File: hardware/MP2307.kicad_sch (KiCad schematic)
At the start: 13 parts, among them U5 MP2307DN-LF-Z

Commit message: ldo
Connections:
- net +12V_UPS renamed IN
- net +3.3V_UPS renamed OUT
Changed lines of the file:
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@@
+	)
+	(junction
+		(at 83.82 67.31)
+		(diameter 0)
+		(color 0 0 0 0)
 	)
 	(junction
@@
 	)
 	(junction
-		(at 128.27 67.31)
-		(diameter 0)
-		(color 0 0 0 0)
-	)
-	(junction
 		(at 152.4 83.82)
 		(diameter 0)
@@
 	(wire
 		(pts
-			(xy 128.27 63.5) (xy 128.27 67.31)
+			(xy 74.93 67.31) (xy 83.82 67.31)
 		)
 		(stroke
@@
 			(width 0)
 			(type default)
+		)
+	)
+	(hierarchical_label "OUT"
+		(shape output)
+		(at 194.31 80.01 0)
+		(effects
+			(font
+				(size 1.27 1.27)
+			)
+			(justify left)
+		)
+	)
+	(hierarchical_label "IN"
+		(shape input)
+		(at 74.93 67.31 180)
+		(effects
+			(font
+				(size 1.27 1.27)
+			)
+			(justify right)
 		)
 	)
@@
 	)
 	(symbol
-		(lib_id "power:+12V")
-		(at 128.27 63.5 0)
-		(unit 1)
-		(exclude_from_sim no)
-		(in_bom yes)
-		(on_board yes)
-		(dnp no)
-		(property "Reference" "#PWR018"
-			(at 128.27 67.31 0)
-			(effects
-				(font
-					(size 1.27 1.27)
-				)
-				(hide yes)
-			)
-		)
-		(property "Value" "+12V_UPS"
-			(at 117.094 61.976 0)
-			(effects
-				(font
-					(size 1.27 1.27)
-				)
-				(justify left)
-			)
-		)
-		(property "Footprint" ""
-			(at 128.27 63.5 0)
-			(effects
-				(font
-					(size 1.27 1.27)
-				)
-				(hide yes)
-			)
-		)
-		(property "Datasheet" ""
-			(at 128.27 63.5 0)
-			(effects
-				(font
-					(size 1.27 1.27)
-				)
-				(hide yes)
-			)
-		)
-		(property "Description" "Power symbol creates a global label with name \"+12V\""
-			(at 128.27 63.5 0)
-			(effects
-				(font
-					(size 1.27 1.27)
-				)
-				(hide yes)
-			)
-		)
-		(pin "1"
-		)
-		(instances
-			(project "NosVolt"
-				(path "/2a3ef4c2-927a-45cd-a4f2-5ee83a7e9444/32fe5c1b-d6e5-49ce-a57a-909ff60d86f6"
-					(reference "#PWR018")
-					(unit 1)
-				)
-			)
-		)
-	)
-	(symbol
 		(lib_id "Device:R")
 		(at 152.4 92.71 180)
@@
 	)
 	(symbol
-		(lib_id "power:+3.3V")
-		(at 194.31 80.01 270)
-		(unit 1)
-		(exclude_from_sim no)
-		(in_bom yes)
-		(on_board yes)
-		(dnp no)
-		(property "Reference" "#PWR022"
-			(at 190.5 80.01 0)
-			(effects
-				(font
-					(size 1.27 1.27)
-				)
-				(hide yes)
-			)
-		)
-		(property "Value" "+3.3V_UPS"
-			(at 188.722 77.216 90)
-			(effects
-				(font
-					(size 1.27 1.27)
-				)
-				(justify left)
+		(lib_id "power:GND")
+		(at 167.64 109.22 0)
+		(unit 1)
+		(exclude_from_sim no)
+		(in_bom yes)
+		(on_board yes)
+		(dnp no)
+		(fields_autoplaced yes)
+		(property "Reference" "#PWR01"
+			(at 167.64 115.57 0)
+			(effects
+				(font
+					(size 1.27 1.27)
+				)
+				(hide yes)
+			)
+		)
+		(property "Value" "GND"
+			(at 167.64 114.3 0)
+			(effects
+				(font
+					(size 1.27 1.27)
+				)
 			)
 		)
 		(property "Footprint" ""
-			(at 194.31 80.01 0)
+			(at 167.64 109.22 0)
 			(effects
 				(font
@@
 		)
 		(property "Datasheet" ""
-			(at 194.31 80.01 0)
-			(effects
-				(font
-					(size 1.27 1.27)
-				)
-				(hide yes)
-			)
-		)
-		(property "Description" "Power symbol creates a global label with name \"+3.3V\""
-			(at 194.31 80.01 0)
-			(effects
-				(font
-					(size 1.27 1.27)
-				)
-				(hide yes)
-			)
-		)
-		(pin "1"
-		)
-		(instances
-			(project "NosVolt"
-				(path "/2a3ef4c2-927a-45cd-a4f2-5ee83a7e9444/32fe5c1b-d6e5-49ce-a57a-909ff60d86f6"
-					(reference "#PWR022")
+			(at 167.64 109.22 0)
+			(effects
+				(font
+					(size 1.27 1.27)
+				)
+				(hide yes)
+			)
+		)
+		(property "Description" "Power symbol creates a global label with name \"GND\" , ground"
+			(at 167.64 109.22 0)
+			(effects
+				(font
+					(size 1.27 1.27)
+				)
+				(hide yes)
+			)
+		)
+		(pin "1"
+		)
+		(instances
+			(project "NosVolt"
+				(path "/2a3ef4c2-927a-45cd-a4f2-5ee83a7e9444/32fe5c1b-d6e5-49ce-a57a-909ff60d86f6"
+					(reference "#PWR01")
 					(unit 1)
 				)
@@
 					(unit 1)
 				)
-			)
-		)
-	)
-	(symbol
-		(lib_id "power:GND")
-		(at 167.64 109.22 0)
-		(unit 1)
-		(exclude_from_sim no)
-		(in_bom yes)
-		(on_board yes)
-		(dnp no)
-		(fields_autoplaced yes)
-		(property "Reference" "#PWR021"
-			(at 167.64 115.57 0)
-			(effects
-				(font
-					(size 1.27 1.27)
-				)
-				(hide yes)
-			)
-		)
-		(property "Value" "GND"
-			(at 167.64 114.3 0)
-			(effects
-				(font
-					(size 1.27 1.27)
-				)
-			)
-		)
-		(property "Footprint" ""
-			(at 167.64 109.22 0)
-			(effects
-				(font
-					(size 1.27 1.27)
-				)
-				(hide yes)
-			)
-		)
-		(property "Datasheet" ""
-			(at 167.64 109.22 0)
-			(effects
-				(font
-					(size 1.27 1.27)
-				)
-				(hide yes)
-			)
-		)
-		(property "Description" "Power symbol creates a global label with name \"GND\" , ground"
-			(at 167.64 109.22 0)
-			(effects
-				(font
-					(size 1.27 1.27)
-				)
-				(hide yes)
-			)
-		)
-		(pin "1"
-		)
-		(instances
-			(project "NosVolt"
-				(path "/2a3ef4c2-927a-45cd-a4f2-5ee83a7e9444/32fe5c1b-d6e5-49ce-a57a-909ff60d86f6"
-					(reference "#PWR021")
-					(unit 1)
-				)

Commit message: Outputs and current measurement
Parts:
- R301: renamed from R14; footprint Resistor_SMD:R_0603_1608Metric -> Resistor_SMD:R_0603_1608Metric_Pad0.98x0.95mm_HandSolder
- R302: renamed from R15; footprint Resistor_SMD:R_0603_1608Metric -> Resistor_SMD:R_0603_1608Metric_Pad0.98x0.95mm_HandSolder
- R303: renamed from R16; footprint Resistor_SMD:R_0603_1608Metric -> Resistor_SMD:R_0603_1608Metric_Pad0.98x0.95mm_HandSolder
- R304: renamed from R17; footprint Resistor_SMD:R_0603_1608Metric -> Resistor_SMD:R_0603_1608Metric_Pad0.98x0.95mm_HandSolder
- U301: renamed from U5; footprint Package_SO:SOIC-8-1EP_3.9x4.9mm_P1.27mm_EP2.29x3mm_ThermalVias -> Package_SO:SOIC-8-1EP_3.9x4.9mm_P1.27mm_EP2.29x3mm
- renumbered C13 to C301, C14 to C302, C15 to C303, C16 to C304, C17 to C305, C18 to C306, C19 to C307, L1 to L301
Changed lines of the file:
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@@
 		(on_board yes)
 		(dnp no)
-		(property "Reference" "C16"
+		(property "Reference" "C304"
 			(at 130.81 95.758 0)
 			(effects
@@
 			(project "NosVolt"
 				(path "/2a3ef4c2-927a-45cd-a4f2-5ee83a7e9444/32fe5c1b-d6e5-49ce-a57a-909ff60d86f6"
-					(reference "C16")
+					(reference "C304")
 					(unit 1)
 				)
@@
 		(on_board yes)
 		(dnp no)
-		(property "Reference" "R14"
+		(property "Reference" "R301"
 			(at 114.3 71.374 90)
 			(effects
@@
 			)
 		)
-		(property "Footprint" "Resistor_SMD:R_0603_1608Metric"
+		(property "Footprint" "Resistor_SMD:R_0603_1608Metric_Pad0.98x0.95mm_HandSolder"
 			(at 114.3 77.978 90)
 			(effects
@@
 			(project "NosVolt"
 				(path "/2a3ef4c2-927a-45cd-a4f2-5ee83a7e9444/32fe5c1b-d6e5-49ce-a57a-909ff60d86f6"
-					(reference "R14")
+					(reference "R301")
 					(unit 1)
 				)
@@
 		(dnp no)
 		(fields_autoplaced yes)
-		(property "Reference" "#PWR019"
+		(property "Reference" "#PWR0304"
 			(at 128.27 115.57 0)
 			(effects
@@
 			(project "NosVolt"
 				(path "/2a3ef4c2-927a-45cd-a4f2-5ee83a7e9444/32fe5c1b-d6e5-49ce-a57a-909ff60d86f6"
-					(reference "#PWR019")
+					(reference "#PWR0304")
 					(unit 1)
 				)
@@
 		(dnp no)
 		(fields_autoplaced yes)
-		(property "Reference" "#PWR017"
+		(property "Reference" "#PWR0303"
 			(at 107.95 115.57 0)
 			(effects
@@
 			(project "NosVolt"
 				(path "/2a3ef4c2-927a-45cd-a4f2-5ee83a7e9444/32fe5c1b-d6e5-49ce-a57a-909ff60d86f6"
-					(reference "#PWR017")
+					(reference "#PWR0303")
 					(unit 1)
 				)
@@
 		(dnp no)
 		(fields_autoplaced yes)
-		(property "Reference" "C17"
+		(property "Reference" "C305"
 			(at 154.94 68.58 90)
 			(effects
@@
 			(project "NosVolt"
 				(path "/2a3ef4c2-927a-45cd-a4f2-5ee83a7e9444/32fe5c1b-d6e5-49ce-a57a-909ff60d86f6"
-					(reference "C17")
+					(reference "C305")
 					(unit 1)
 				)
@@
 		(dnp no)
 		(fields_autoplaced yes)
-		(property "Reference" "C13"
+		(property "Reference" "C301"
 			(at 87.63 86.3599 0)
 			(effects
@@
 			(project "NosVolt"
 				(path "/2a3ef4c2-927a-45cd-a4f2-5ee83a7e9444/32fe5c1b-d6e5-49ce-a57a-909ff60d86f6"
-					(reference "C13")
+					(reference "C301")
 					(unit 1)
 				)
@@
 		(dnp no)
 		(fields_autoplaced yes)
-		(property "Reference" "L1"
+		(property "Reference" "L301"
 			(at 177.8 74.93 90)
 			(effects
@@
 			(project "NosVolt"
 				(path "/2a3ef4c2-927a-45cd-a4f2-5ee83a7e9444/32fe5c1b-d6e5-49ce-a57a-909ff60d86f6"
-					(reference "L1")
+					(reference "L301")
 					(unit 1)
 				)
@@
 		(on_board yes)
 		(dnp no)
-		(property "Reference" "R15"
+		(property "Reference" "R302"
 			(at 134.62 105.156 0)
 			(effects
@@
 			)
 		)
-		(property "Footprint" "Resistor_SMD:R_0603_1608Metric"
+		(property "Footprint" "Resistor_SMD:R_0603_1608Metric_Pad0.98x0.95mm_HandSolder"
 			(at 140.208 104.14 90)
 			(effects
@@
 			(project "NosVolt"
 				(path "/2a3ef4c2-927a-45cd-a4f2-5ee83a7e9444/32fe5c1b-d6e5-49ce-a57a-909ff60d86f6"
-					(reference "R15")
+					(reference "R302")
 					(unit 1)
 				)
@@
 		(on_board yes)
 		(dnp no)
-		(property "Reference" "R16"
+		(property "Reference" "R303"
 			(at 148.082 93.98 0)
 			(effects
@@
 			)
 		)
-		(property "Footprint" "Resistor_SMD:R_0603_1608Metric"
+		(property "Footprint" "Resistor_SMD:R_0603_1608Metric_Pad0.98x0.95mm_HandSolder"
 			(at 154.178 92.71 90)
 			(effects
@@
 			(project "NosVolt"
 				(path "/2a3ef4c2-927a-45cd-a4f2-5ee83a7e9444/32fe5c1b-d6e5-49ce-a57a-909ff60d86f6"
-					(reference "R16")
+					(reference "R303")
 					(unit 1)
 				)
@@
 		(dnp no)
 		(fields_autoplaced yes)
-		(property "Reference" "#PWR01"
+		(property "Reference" "#PWR0306"
 			(at 167.64 115.57 0)
 			(effects
@@
 			(project "NosVolt"
 				(path "/2a3ef4c2-927a-45cd-a4f2-5ee83a7e9444/32fe5c1b-d6e5-49ce-a57a-909ff60d86f6"
-					(reference "#PWR01")
+					(reference "#PWR0306")
 					(unit 1)
 				)
@@
 		(dnp no)
 		(fields_autoplaced yes)
-		(property "Reference" "#PWR016"
+		(property "Reference" "#PWR0302"
 			(at 95.25 115.57 0)
 			(effects
@@
 			(project "NosVolt"
 				(path "/2a3ef4c2-927a-45cd-a4f2-5ee83a7e9444/32fe5c1b-d6e5-49ce-a57a-909ff60d86f6"
-					(reference "#PWR016")
+					(reference "#PWR0302")
 					(unit 1)
 				)
@@
 		(dnp no)
 		(fields_autoplaced yes)
-		(property "Reference" "#PWR015"
+		(property "Reference" "#PWR0301"
 			(at 83.82 115.57 0)
 			(effects
@@
 			(project "NosVolt"
 				(path "/2a3ef4c2-927a-45cd-a4f2-5ee83a7e9444/32fe5c1b-d6e5-49ce-a57a-909ff60d86f6"
-					(reference "#PWR015")
+					(reference "#PWR0301")
 					(unit 1)
 				)
@@
 		(dnp no)
 		(fields_autoplaced yes)
-		(property "Reference" "C14"
+		(property "Reference" "C302"
 			(at 99.06 86.3599 0)
 			(effects
@@
 			(project "NosVolt"
 				(path "/2a3ef4c2-927a-45cd-a4f2-5ee83a7e9444/32fe5c1b-d6e5-49ce-a57a-909ff60d86f6"
-					(reference "C14")
+					(reference "C302")
 					(unit 1)
 				)
@@
 		(dnp no)
 		(fields_autoplaced yes)
-		(property "Reference" "#PWR020"
+		(property "Reference" "#PWR0305"
 			(at 138.43 115.57 0)
 			(effects
@@
 			(project "NosVolt"
 				(path "/2a3ef4c2-927a-45cd-a4f2-5ee83a7e9444/32fe5c1b-d6e5-49ce-a57a-909ff60d86f6"
-					(reference "#PWR020")
+					(reference "#PWR0305")
 					(unit 1)
 				)
@@
 		(dnp no)
 		(fields_autoplaced yes)
-		(property "Reference" "C19"
+		(property "Reference" "C307"
 			(at 190.5 91.4399 0)
 			(effects
@@
 			(project "NosVolt"
 				(path "/2a3ef4c2-927a-45cd-a4f2-5ee83a7e9444/32fe5c1b-d6e5-49ce-a57a-909ff60d86f6"
-					(reference "C19")
+					(reference "C307")
 					(unit 1)
 				)
@@
 		(dnp no)
 		(fields_autoplaced yes)
-		(property "Reference" "C15"
+		(property "Reference" "C303"
 			(at 111.76 95.2499 0)
 			(effects
@@
 			(project "NosVolt"
 				(path "/2a3ef4c2-927a-45cd-a4f2-5ee83a7e9444/32fe5c1b-d6e5-49ce-a57a-909ff60d86f6"
-					(reference "C15")
+					(reference "C303")
 					(unit 1)
 				)
@@
 		(dnp no)
 		(fields_autoplaced yes)
-		(property "Reference" "C18"
+		(property "Reference" "C306"
 			(at 171.45 91.4399 0)
 			(effects
@@
 			(project "NosVolt"
 				(path "/2a3ef4c2-927a-45cd-a4f2-5ee83a7e9444/32fe5c1b-d6e5-49ce-a57a-909ff60d86f6"
-					(reference "C18")
+					(reference "C306")
 					(unit 1)
 				)
@@
 		(on_board yes)
 		(dnp no)
-		(property "Reference" "U5"
+		(property "Reference" "U301"
 			(at 135.128 67.564 0)
 			(effects
@@
 			)
 		)
-		(property "Footprint" "Package_SO:SOIC-8-1EP_3.9x4.9mm_P1.27mm_EP2.29x3mm_ThermalVias"
+		(property "Footprint" "Package_SO:SOIC-8-1EP_3.9x4.9mm_P1.27mm_EP2.29x3mm"
 			(at 141.224 42.926 0)
 			(effects
@@
 			(project "NosVolt"
 				(path "/2a3ef4c2-927a-45cd-a4f2-5ee83a7e9444/32fe5c1b-d6e5-49ce-a57a-909ff60d86f6"
-					(reference "U5")
+					(reference "U301")
 					(unit 1)
 				)
@@
 		(on_board yes)
 		(dnp no)
-		(property "Reference" "R17"
+		(property "Reference" "R304"
 			(at 160.274 86.36 90)
 			(effects
@@
 			)
 		)
-		(property "Footprint" "Resistor_SMD:R_0603_1608Metric"
+		(property "Footprint" "Resistor_SMD:R_0603_1608Metric_Pad0.98x0.95mm_HandSolder"
 			(at 160.02 85.598 90)
 			(effects
@@
 			(project "NosVolt"
 				(path "/2a3ef4c2-927a-45cd-a4f2-5ee83a7e9444/32fe5c1b-d6e5-49ce-a57a-909ff60d86f6"
-					(reference "R17")
-					(unit 1)
-				)
+					(reference "R304")
+					(unit 1)
+				)

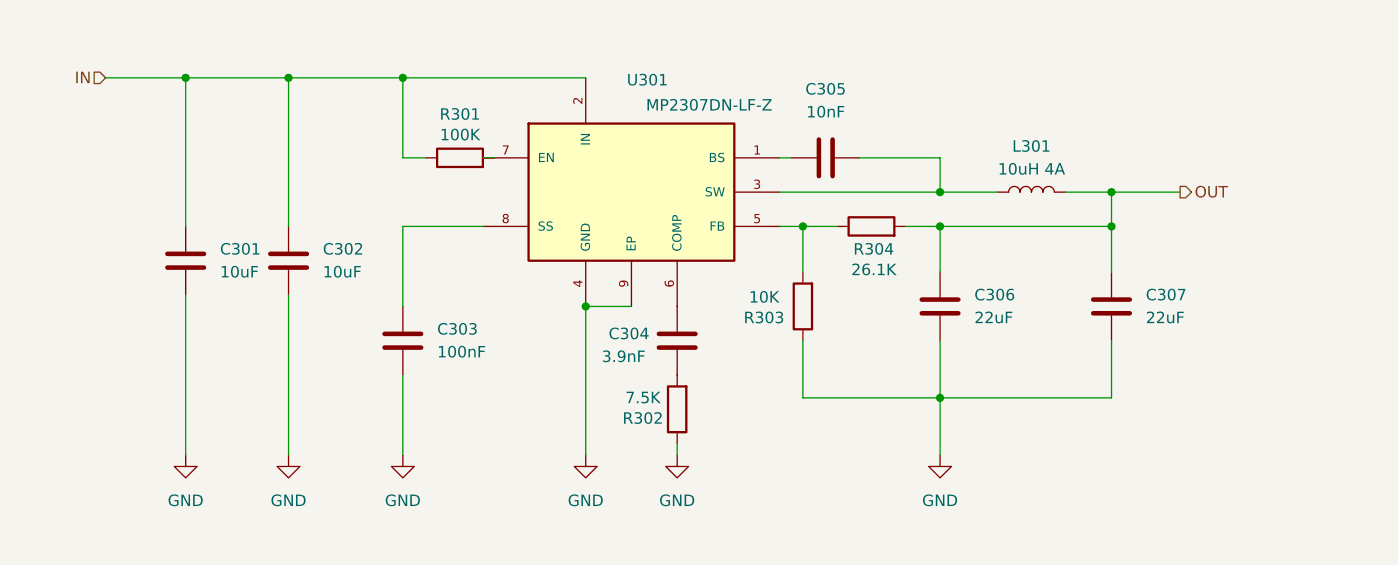
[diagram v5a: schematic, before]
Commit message: thermal relief
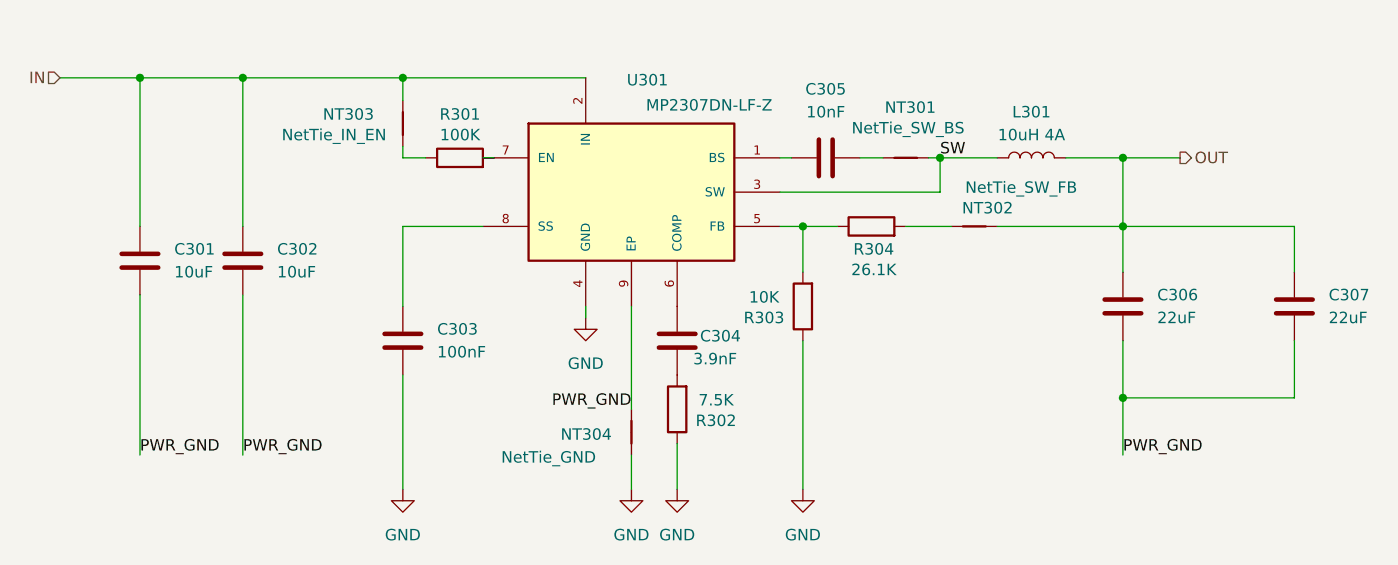
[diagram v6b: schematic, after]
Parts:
- added NT301: NetTie_SW_BS, NetTie:NetTie-2_SMD_Pad0.5mm, symbol Device:NetTie_2
- added NT302: NetTie_SW_FB, NetTie:NetTie-2_SMD_Pad0.5mm, symbol Device:NetTie_2
- added NT303: NetTie_IN_EN, NetTie:NetTie-2_SMD_Pad0.5mm, symbol Device:NetTie_2
- added NT304: NetTie_GND, NetTie:NetTie-2_SMD_Pad0.5mm, symbol Device:NetTie_2
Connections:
- net GND: now also NT304.1; no longer C301.2, C302.2, C306.2, C307.2, U301.9 (EP)
- net IN: now also NT303.1; no longer R301.1
- net OUT: now also NT302.2; no longer R304.2
- net SW: now reaches L301.1, U301.3 (SW)
- net SW: now also NT301.2; no longer C305.2
- new net: NT303.2, R301.1
- new net: C305.2, NT301.1
- new net: NT302.1, R304.2
- new net PWR_GND: C301.2, C302.2, C306.2, C307.2, NT304.2, U301.9 (EP)
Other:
- moved on the sheet: C301, C302, C306, C307, L301

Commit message: tracing
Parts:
- U301: footprint Package_SO:SOIC-8-1EP_3.9x4.9mm_P1.27mm_EP2.29x3mm -> Package_SO:SOIC-8-1EP_3.9x4.9mm_P1.27mm_EP2.29x3mm_ThermalVias
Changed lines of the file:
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@@
 			)
 		)
-		(property "Footprint" "Package_SO:SOIC-8-1EP_3.9x4.9mm_P1.27mm_EP2.29x3mm"
+		(property "Footprint" "Package_SO:SOIC-8-1EP_3.9x4.9mm_P1.27mm_EP2.29x3mm_ThermalVias"
 			(at 141.224 42.926 0)
 			(effects
